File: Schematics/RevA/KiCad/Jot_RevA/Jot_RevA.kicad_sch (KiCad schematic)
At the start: 0 parts

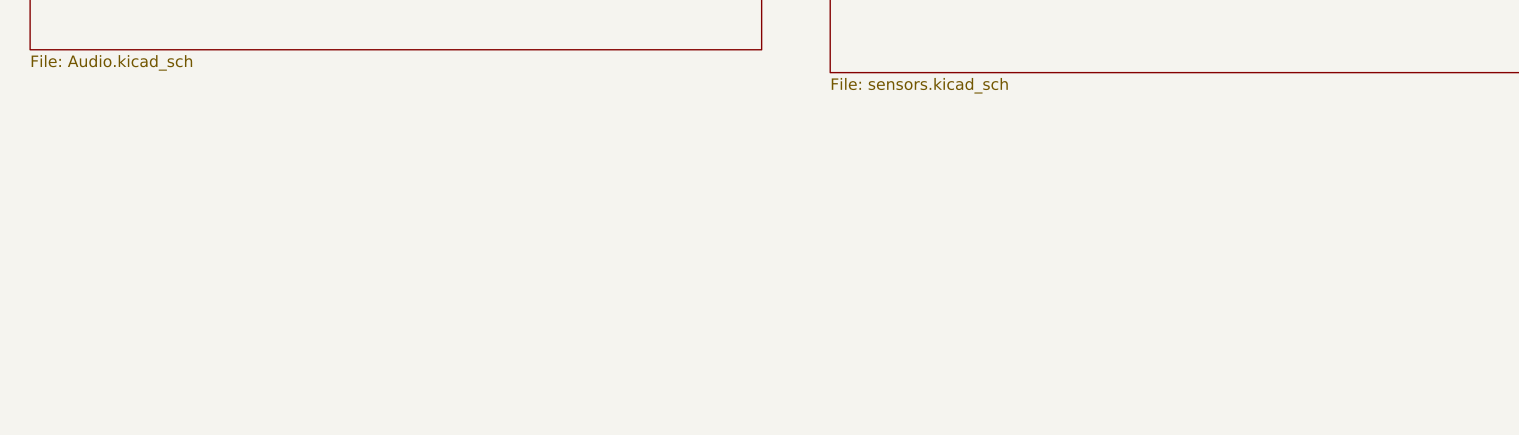
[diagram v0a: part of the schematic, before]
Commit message: NFC sheet: new sheet with NFC1/NFC2 labels and title block; title blocks restored after an editor overwrite; MCU NFC2 label tidied
Co-Authored-By: Claude Opus 5.5 <noreply@anthropic.com>
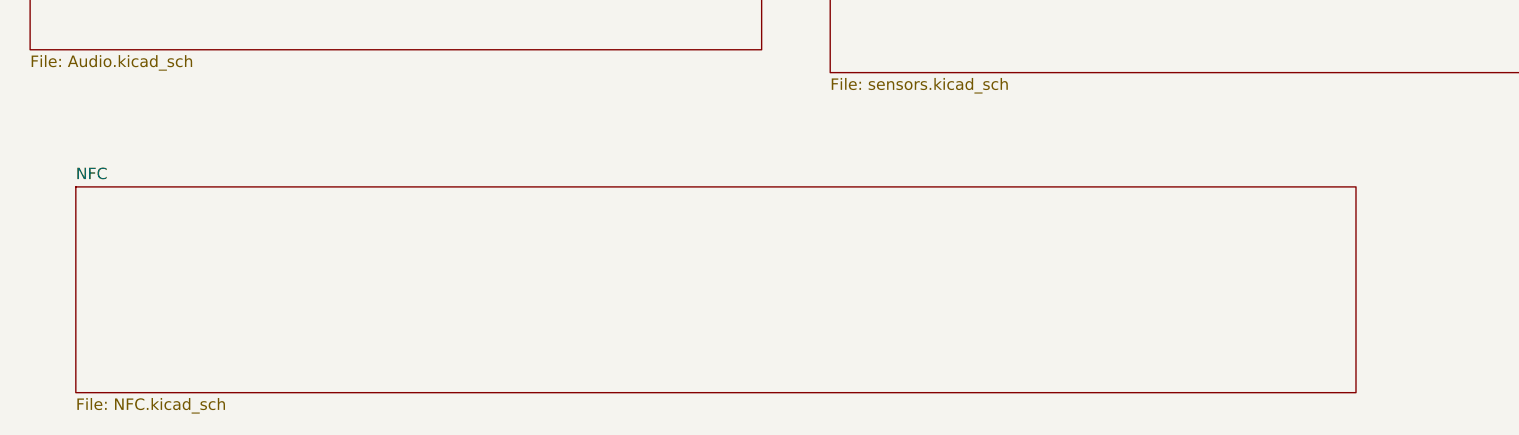
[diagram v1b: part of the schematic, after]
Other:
- added sheet NFC (NFC.kicad_sch)
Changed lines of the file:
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@@
+	)
+	(sheet
+		(at 20.32 167.64)
+		(size 142.24 22.86)
+		(exclude_from_sim no)
+		(in_bom yes)
+		(on_board yes)
+		(dnp no)
+		(fields_autoplaced yes)
+		(stroke
+			(width 0.1524)
+			(type solid)
+		)
+		(fill
+			(color 0 0 0 0)
+		)
+		(property "Sheetname" "NFC"
+			(at 20.32 166.9284 0)
+			(show_name no)
+			(do_not_autoplace no)
+			(effects
+				(font
+					(size 1.27 1.27)
+				)
+				(justify left bottom)
+			)
+		)
+		(property "Sheetfile" "NFC.kicad_sch"
+			(at 20.32 191.0846 0)
+			(show_name no)
+			(do_not_autoplace no)
+			(effects
+				(font
+					(size 1.27 1.27)
+				)
+				(justify left top)
+			)
+		)
+		(instances
+			(project "Jot_RevA"
+				(path "/61747270-9f90-47b6-9c50-5ea1f41f259a"
+					(page "9")
+				)
+			)
+		)
 	)
 	(sheet
